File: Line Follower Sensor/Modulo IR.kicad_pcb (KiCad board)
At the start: 2 copper layers, 17.5 x 36.6 mm, 12 parts, among them U1 LM358N, U10 100nF, U12 TCRT5000, U13 100R, U3 1K, U5 20K, U6 10K, U7 POT, U8 CON3_ET, U9 LED

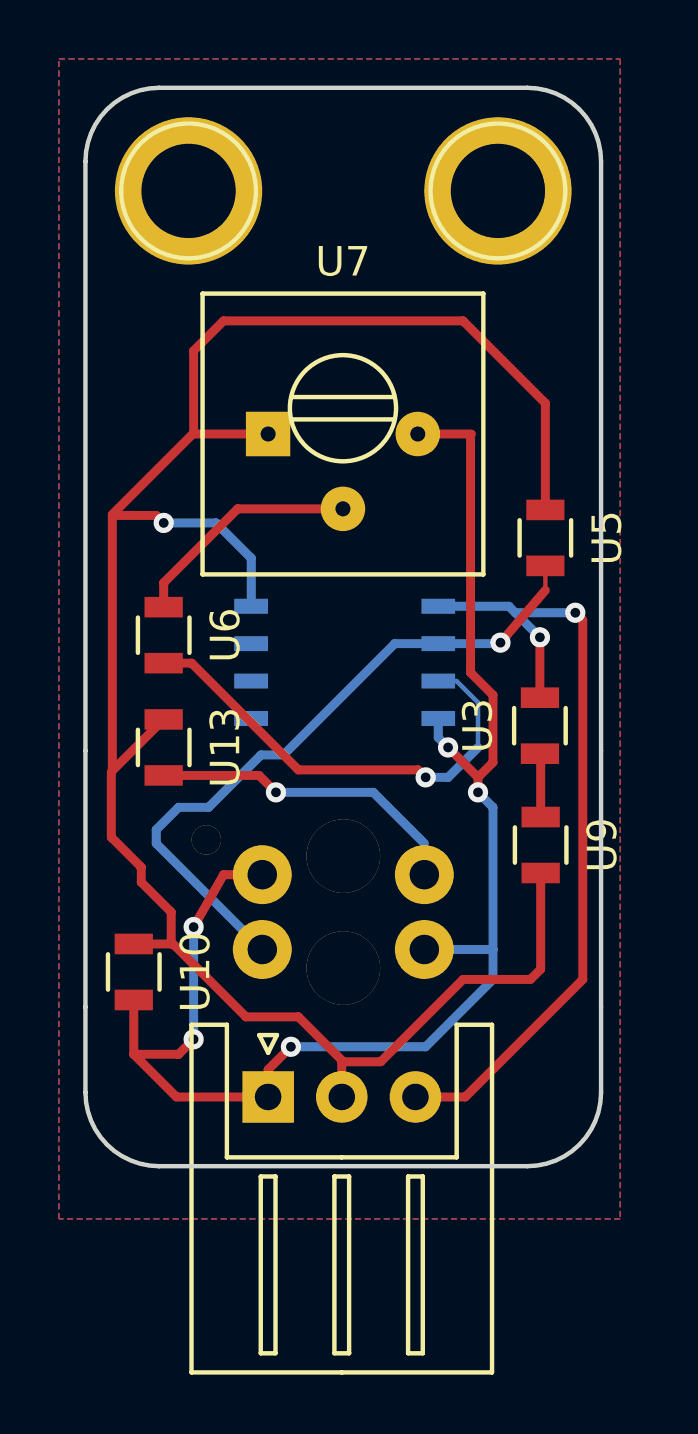
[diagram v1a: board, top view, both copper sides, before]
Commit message: Componentes colocados
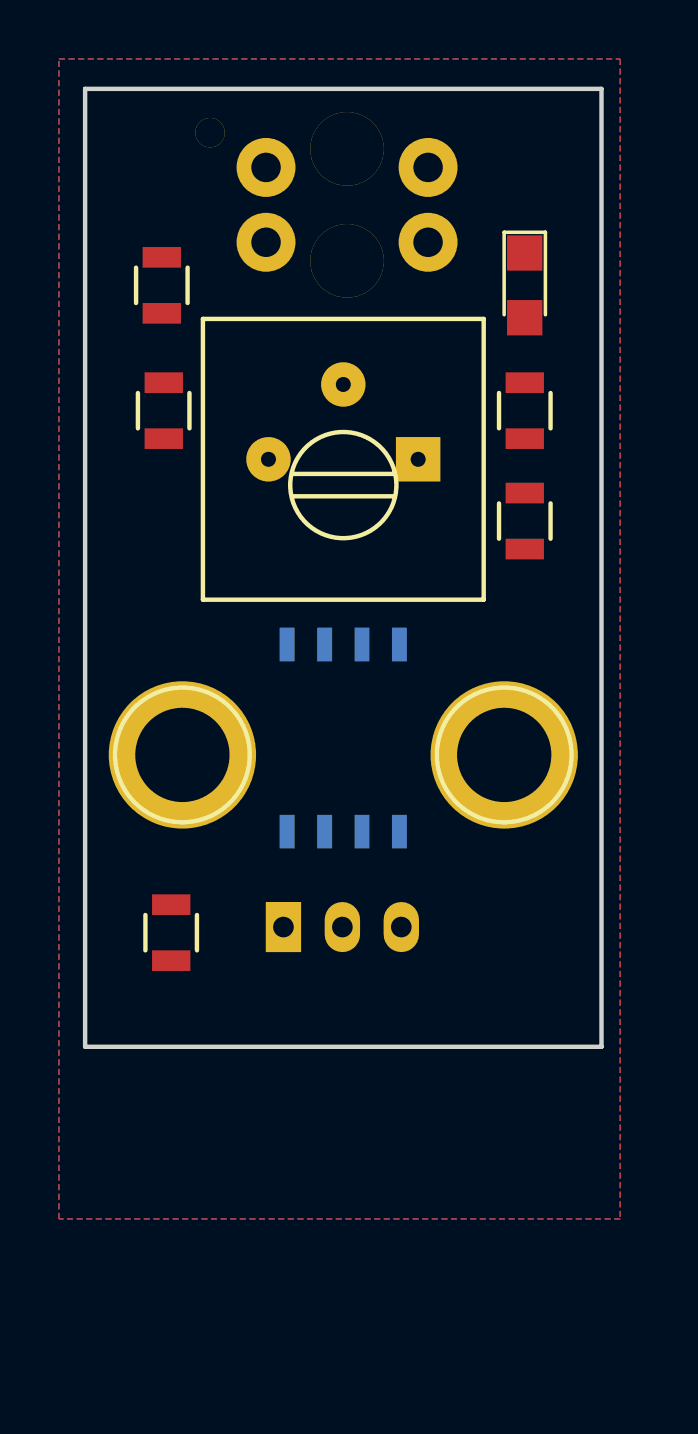
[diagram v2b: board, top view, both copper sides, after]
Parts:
- U7: value POT -> 10k
- U8: footprint Connectors_JST:JST_XH_S03B-XH-A_03x2.50mm_Angled -> Connectors_JST:JST_PH_S3B-PH-K_03x2.00mm_Angled
- U9: footprint Resistors_SMD:R_0805 -> LEDs:LED_0805
- moved U12 24.0 mm to (111.4, 101.5)
- moved U3 19.7 mm to (105.1, 104.2), turned to 270 degrees
- moved REF** 19.1 mm to (116.7, 120.1)
- moved REF** 19.1 mm to (105.8, 120.1)
- moved U9 19.0 mm to (117.4, 104.2)
- moved U13 16.8 mm to (117.4, 108.5), turned to 90 degrees
- moved U6 7.62 mm to (105.2, 108.5)
- moved U8 5.79 mm to (109.2, 126.0)
- moved U7 5.16 mm to (113.8, 110.1), turned to 180 degrees
- moved U1 2.57 mm to (111.3, 119.6), turned to 180 degrees
- moved U10 1.84 mm to (105.4, 126.2)
- moved U5 0.90 mm to (117.4, 112.2)
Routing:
- net VCC: track 72.5 -> 0.00 mm, vias 1 -> 0
- net GNDREF: track 52.2 -> 0.00 mm, vias 6 -> 0
- net Net-(U1-Pad1): track 27.9 -> 0.00 mm, vias 2 -> 0
- net A0: track 23.0 -> 0.00 mm, vias 1 -> 0
- net Net-(U1-Pad3): track 15.9 -> 0.00 mm, vias 1 -> 0
- net Net-(U12-Pad2): track 10.9 -> 0.00 mm, vias 1 -> 0
- net Net-(U6-Pad1): track 7.95 -> 0.00 mm
- net Net-(U3-Pad1): track 2.16 -> 0.00 mm
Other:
- board size 17.5 x 36.6 mm -> 17.5 x 32.5 mm

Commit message: Serigrafia realizada y placa mandada a fabrica
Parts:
- removed the REF** at (116.7, 120.1)
- removed the REF** at (105.8, 120.1)
- added G***: LOGO, logos_frizzy:logo_lf, F.Cu at (153.2, 100.8)
- added REF**: MountingHole_3.2mm_M3, Mounting_Holes:MountingHole_3.2mm_M3, F.Cu at (158.5, 101.9)
- added REF**: MountingHole_3.2mm_M3, Mounting_Holes:MountingHole_3.2mm_M3, F.Cu at (147.8, 101.9)
- moved U3 56.8 mm to (160.0, 89.9)
- moved U13 49.9 mm to (159.3, 81.3), turned to 180 degrees
- moved U9 46.8 mm to (160.0, 84.8), turned to 90 degrees
- moved U5 46.3 mm to (160.0, 94.0), turned to 90 degrees
- moved U1 45.9 mm to (153.2, 100.8)
- moved U10 45.9 mm to (147.3, 107.4)
- moved U7 45.9 mm to (155.7, 91.3)
- moved U8 45.9 mm to (151.1, 107.2)
- moved U12 45.9 mm to (153.3, 82.7)
- moved U6 44.1 mm to (146.8, 94.0)
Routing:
- net VCC: track 0.00 -> 50.0 mm, vias 0 -> 2
- net A0: track 0.00 -> 30.6 mm, vias 0 -> 1
- net GNDREF: track 0.00 -> 25.5 mm
- net Net-(U1-Pad1): track 0.00 -> 19.0 mm, vias 0 -> 1
- net Net-(U1-Pad3): track 0.00 -> 12.2 mm, vias 0 -> 1
- net Net-(U6-Pad1): track 0.00 -> 9.73 mm
- net Net-(U3-Pad1): track 0.00 -> 3.03 mm
- net Net-(U12-Pad2): track 0.00 -> 2.32 mm
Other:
- board size 17.5 x 32.5 mm -> 17.3 x 32.5 mm
